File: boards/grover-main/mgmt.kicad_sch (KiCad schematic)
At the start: 82 parts

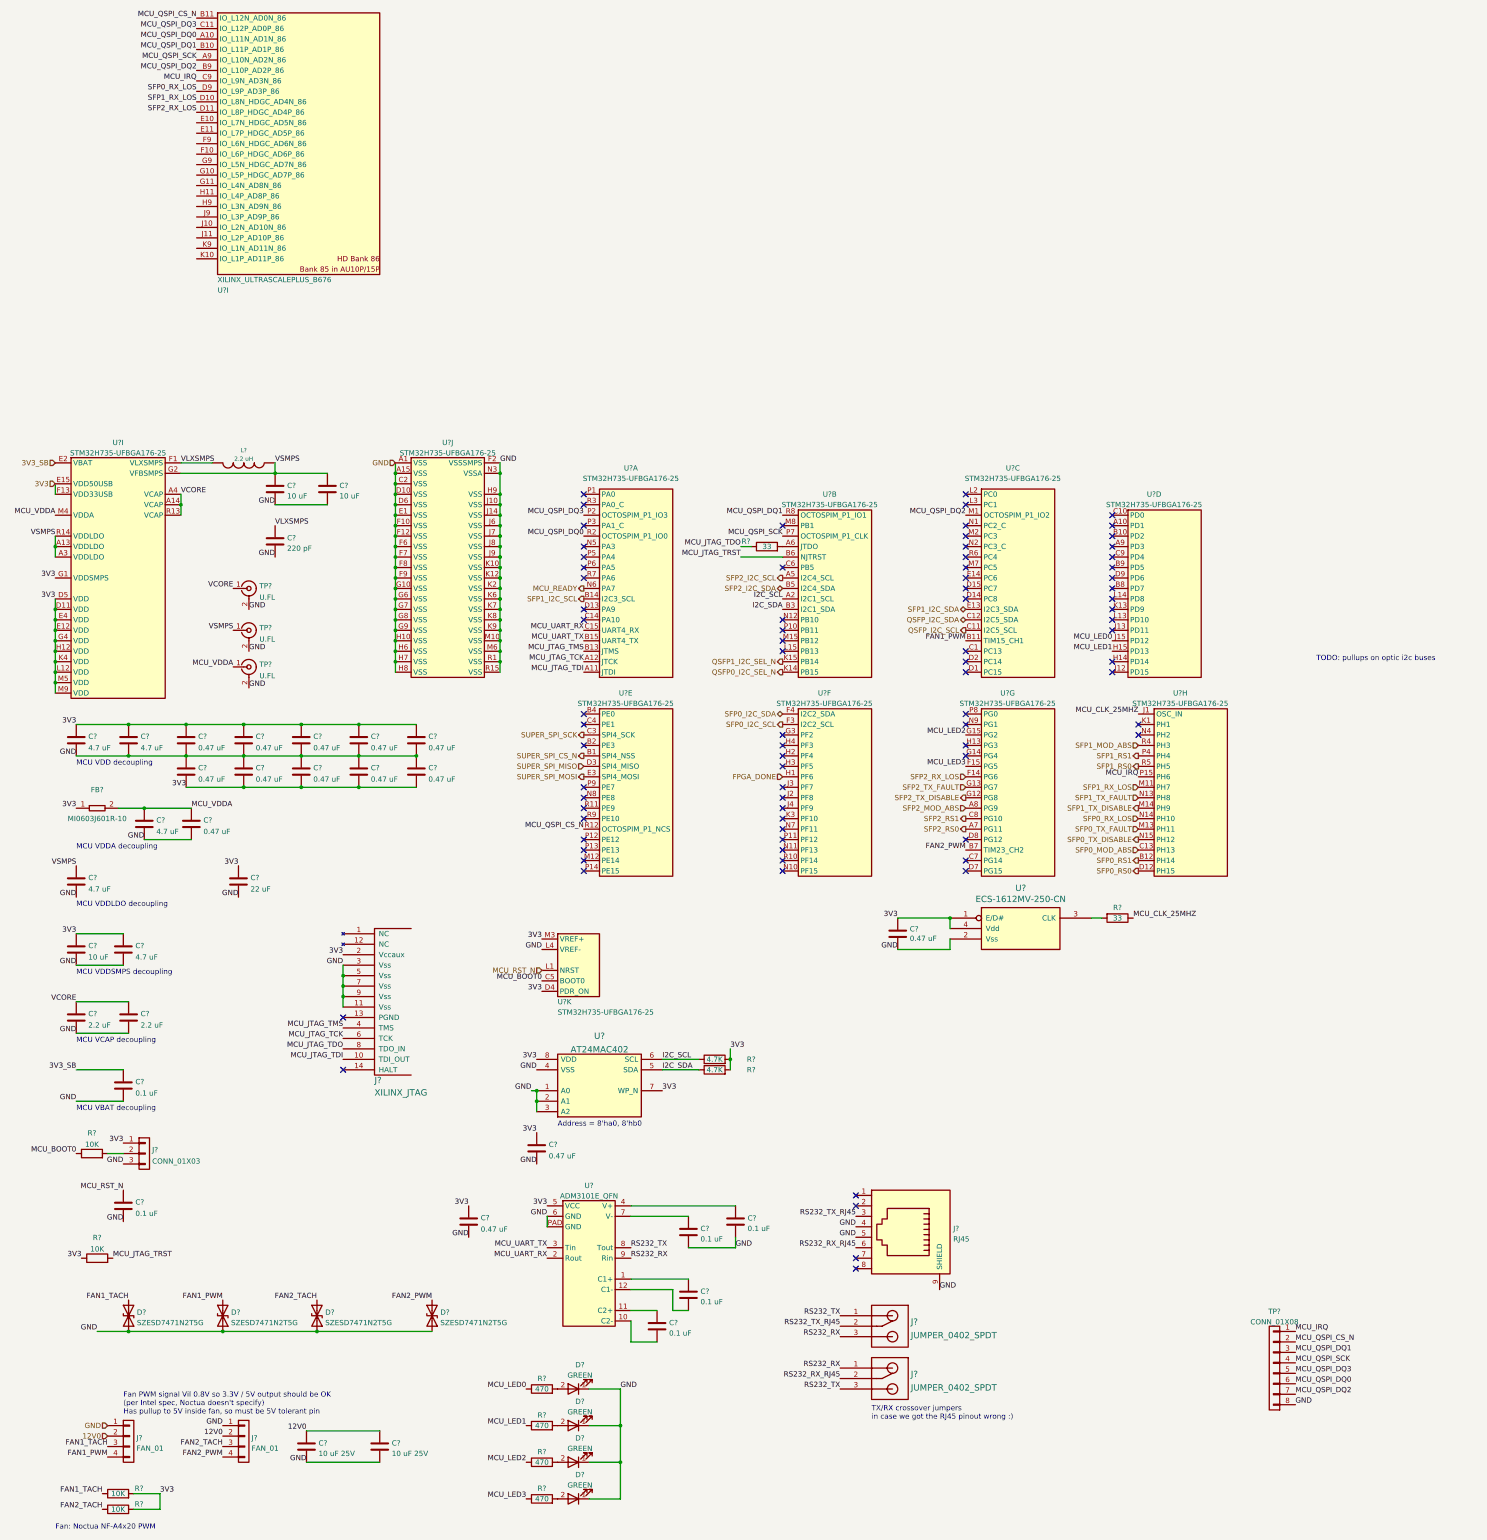
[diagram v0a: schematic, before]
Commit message: Continued initial schematic capture
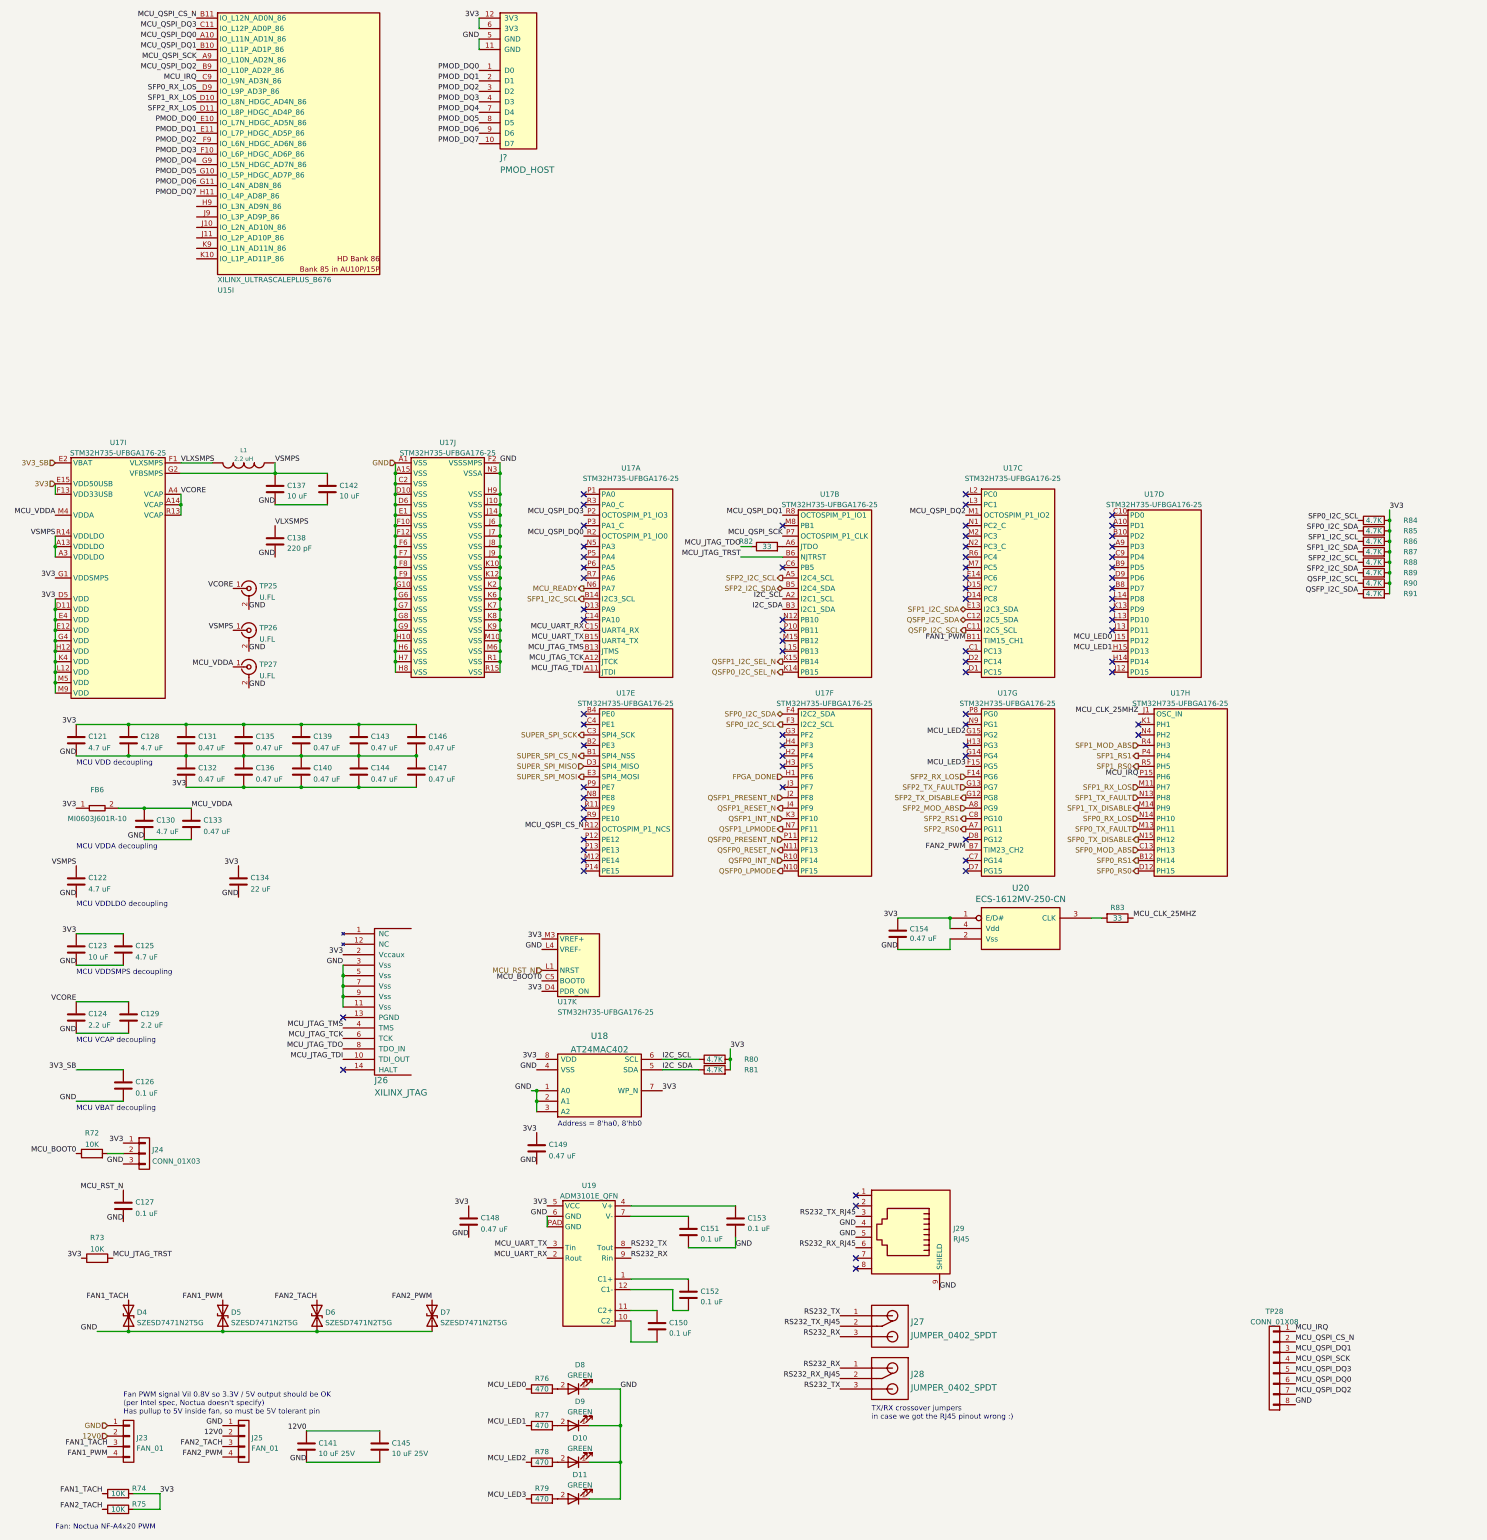
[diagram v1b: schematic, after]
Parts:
- added J?: PMOD_HOST, azonenberg_pcb:CONN_HEADER_2.54MM_2x6_RA_PMOD_HOST, symbol special-azonenberg:PMOD_HOST
- added R84, R85, R86, R87, R88, R89, R90, R91: 4.7K, azonenberg_pcb:EIA_0402_RES_NOSILK, symbol device:R
- gave numbers to parts that had none: 72
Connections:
- net 3V3: now also J?.12 (3V3), J?.6 (3V3), R84.2, R85.2, R86.2, R87.2, R88.2, R89.2, R90.2, R91.2
- net GND: now also J?.11 (GND), J?.5 (GND)
- net QSFP_I2C_SCL: now also R90.1
- net QSFP_I2C_SDA: now also R91.1
- net SFP0_I2C_SCL: now also R84.1
- net SFP0_I2C_SDA: now also R85.1
- net SFP1_I2C_SCL: now also R86.1
- net SFP1_I2C_SDA: now also R87.1
- net SFP2_I2C_SCL: now also R88.1
- net SFP2_I2C_SDA: now also R89.1
- net QSFP1_PRESENT_N: now reaches U17.J2 (PF8)
- net QSFP1_RESET_N: now reaches U17.J4 (PF9)
- net QSFP1_INT_N: now reaches U17.K3 (PF10)
- net QSFP0_LPMODE: now reaches U17.N10 (PF15)
- net QSFP0_RESET_N: now reaches U17.N11 (PF13)
- net QSFP1_LPMODE: now reaches U17.N7 (PF11)
- net QSFP0_PRESENT_N: now reaches U17.P11 (PF12)
- net QSFP0_INT_N: now reaches U17.R10 (PF14)
- net PMOD_DQ0: now reaches U15.E10 (IO_L7N_HDGC_AD5N_86)
- net PMOD_DQ0: now also J?.1 (D0)
- net PMOD_DQ1: now reaches U15.E11 (IO_L7P_HDGC_AD5P_86)
- net PMOD_DQ1: now also J?.2 (D1)
- net PMOD_DQ3: now reaches U15.F10 (IO_L6P_HDGC_AD6P_86)
- net PMOD_DQ3: now also J?.4 (D3)
- net PMOD_DQ2: now reaches U15.F9 (IO_L6N_HDGC_AD6N_86)
- net PMOD_DQ2: now also J?.3 (D2)
- net PMOD_DQ5: now reaches U15.G10 (IO_L5P_HDGC_AD7P_86)
- net PMOD_DQ5: now also J?.8 (D5)
- net PMOD_DQ6: now reaches U15.G11 (IO_L4N_AD8N_86)
- net PMOD_DQ6: now also J?.9 (D6)
- net PMOD_DQ4: now reaches U15.G9 (IO_L5N_HDGC_AD7N_86)
- net PMOD_DQ4: now also J?.7 (D4)
- net PMOD_DQ7: now reaches U15.H11 (IO_L4P_AD8P_86)
- net PMOD_DQ7: now also J?.10 (D7)
- no-connect marks 81 -> 73
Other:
- note removed: "TODO: pullups on optic i2c buses"
